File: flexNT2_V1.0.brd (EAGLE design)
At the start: 38 x 5.9 mm, 6 parts, among them U1 NTAG-I2C+

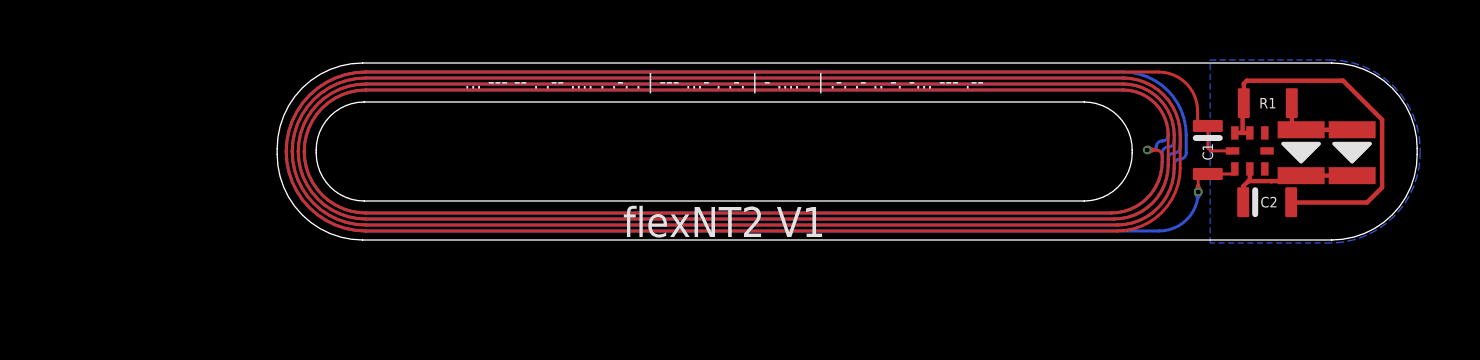
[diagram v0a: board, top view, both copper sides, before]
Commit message: Fixed lib linking and a few other small fixes
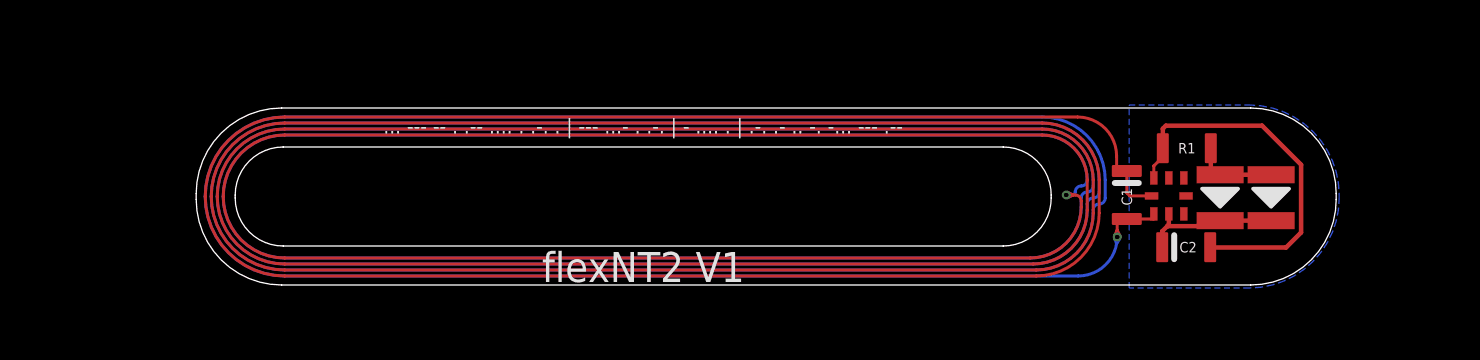
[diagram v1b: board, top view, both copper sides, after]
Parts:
- C1: device Samuel_Collection:0603_FLEX_C_POL -> flexNT2_V1.0:0603_FLEX_C_POL
- C2: value 200pF -> 200nF; device Samuel_Collection:0603_FLEX_C_POL -> flexNT2_V1.0:0603_FLEX_C_POL
- D1, D2: device Samuel_Collection:0807RGBFF_CZINELIGHT -> flexNT2_V1.0:0807RGBFF_CZINELIGHT
- R1: device Samuel_Collection:0603_FLEX -> flexNT2_V1.0:0603_FLEX
- U1: device Samuel_Collection:XQFN8_NTAG-I2C+ -> flexNT2_V1.0:XQFN8_NTAG-I2C+
- moved C2 3.09 mm to (33.0, 1.25)
- moved D2 3.09 mm to (35.8, 2.90)
- moved U1 3.09 mm to (32.4, 2.96)
- moved C1 3.09 mm to (31.0, 2.99)
- moved D1 3.09 mm to (34.1, 2.90)
- moved R1 3.09 mm to (33.0, 4.55)
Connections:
- net VCC: no longer U1.VCC
